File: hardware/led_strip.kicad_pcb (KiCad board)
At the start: 2 copper layers, 30 x 30 mm, 29 parts, among them J1 AKL_5_2, J2 AKL_5_2, J3 AKL_5_2, P1 CON-SENSOR, P2 TST, P3 TST, P4 TST, P5 TST, P6 TST, P7 TST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

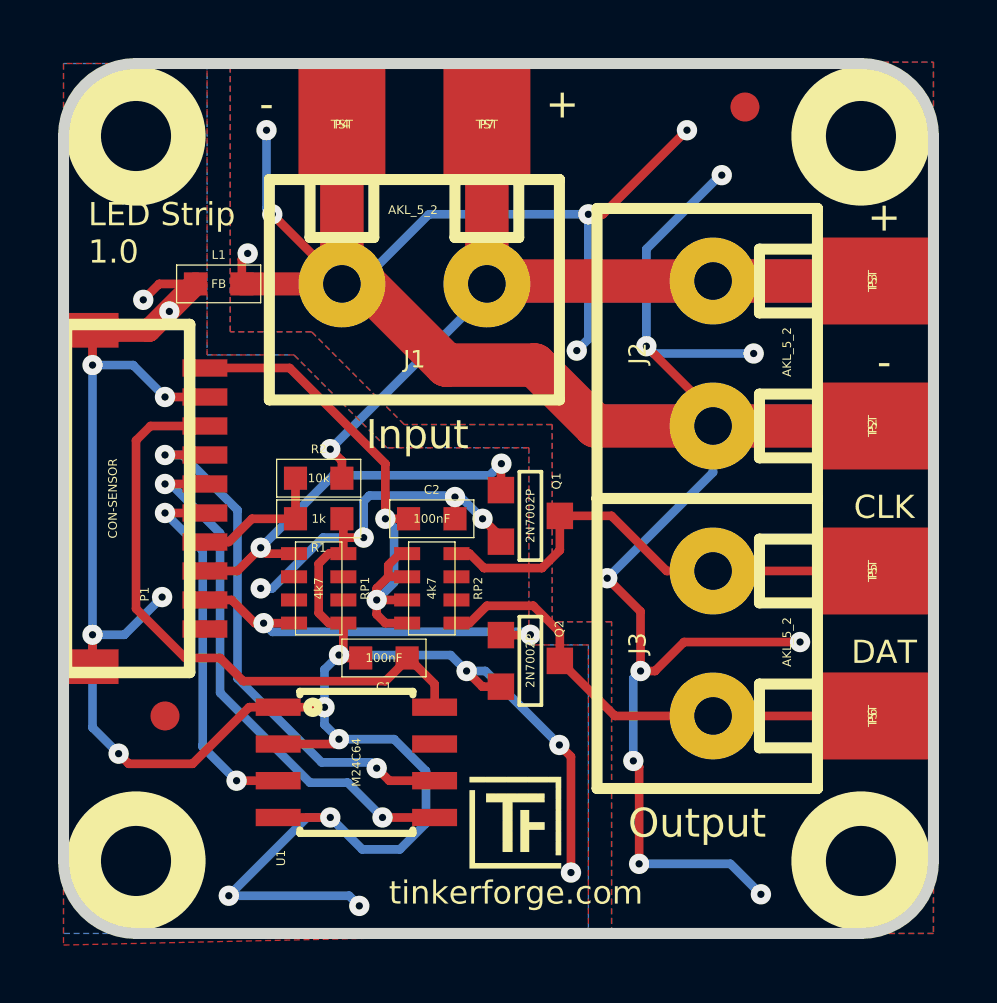
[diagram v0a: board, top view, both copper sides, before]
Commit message: update hardware files with new resistor values
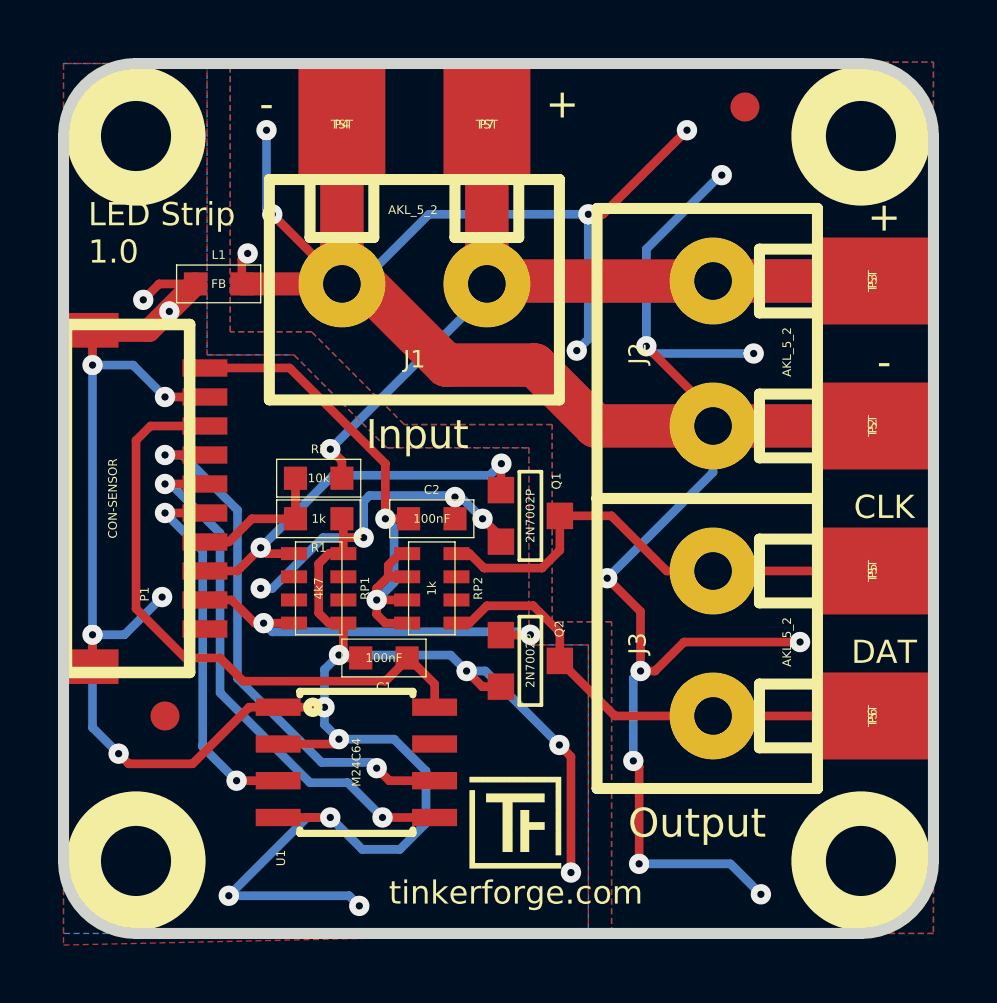
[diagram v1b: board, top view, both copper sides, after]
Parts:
- RP2: value 4k7 -> 1k
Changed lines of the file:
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@@
-(kicad_pcb (version 3) (host pcbnew "(2013-05-18 BZR 4017)-stable")
+(kicad_pcb (version 3) (host pcbnew "(2013-07-24 BZR 4024)-stable")
   (general
     (links 43)
@@
       (effects (font (size 0.29972 0.29972) (thickness 0.0762)))
     )
-    (fp_text value 4k7 (at 0 0 270) (layer F.SilkS)
+    (fp_text value 1k (at 0 0 270) (layer F.SilkS)
       (effects (font (size 0.29972 0.29972) (thickness 0.07493)))
     )

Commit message: new prototype of led strip bricklet
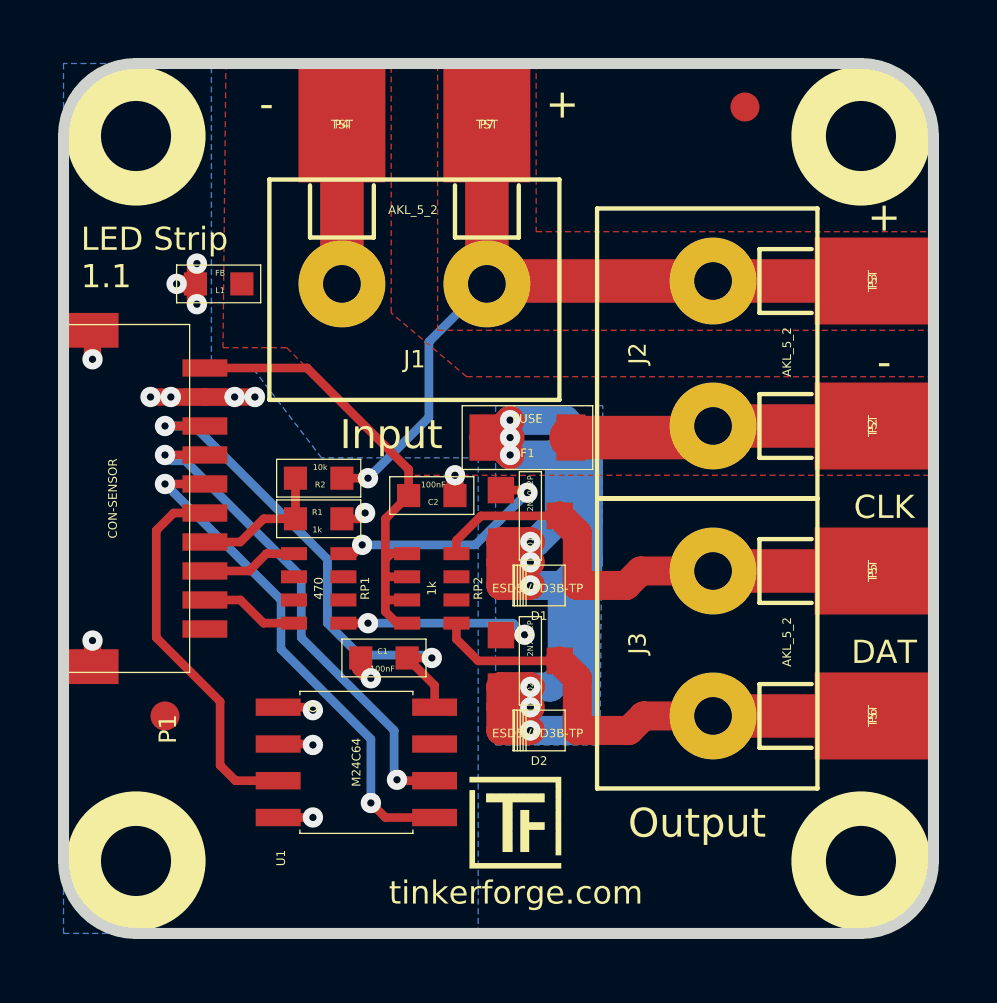
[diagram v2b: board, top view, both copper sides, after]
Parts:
- added D1: ESD5V0D3B-TP, kicad-libraries:SOD-323, F.Cu at (59.3, 45.3)
- added D2: ESD5V0D3B-TP, kicad-libraries:SOD-323, F.Cu at (59.3, 50.3)
- added F1: FUSE, kicad-libraries:1206, F.Cu at (58.9, 40.2)
- C1, C2, L1, R1, R2: footprint 0603 -> kicad-libraries:0603
- J1, J2, J3: footprint AKL_5_2 -> kicad-libraries:AKL_5_2
- P1: footprint CON-SENSOR -> kicad-libraries:CON-SENSOR
- P2, P3, P4, P5, P6, P7: footprint SOLDER_PAD2 -> kicad-libraries:SOLDER_PAD2
- Q1, Q2: footprint SOT23GDS -> kicad-libraries:SOT23GDS
- RP1: value 4k7 -> 470; footprint 4X0603 -> kicad-libraries:4X0603
- RP2: footprint 4X0603 -> kicad-libraries:4X0603
- U1: footprint SOIC8 -> kicad-libraries:SOIC8
- U2, U3, U4, U5: footprint DRILL_NP -> kicad-libraries:DRILL_NP
- moved C2 0.80 mm to (55.6, 42.2)
- moved VAL 0.75 mm to (55.6, 42.3)
- moved VAL 0.20 mm to (61.8, 42.3)
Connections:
- P1 pad 8: N-0000014 -> Net-(P1-Pad8)
- P1 pad 9: N-0000015 -> Net-(P1-Pad9)
- Q1 pad G: N-0000014 -> Net-(Q1-PadG)
- Q1 pad S: GND -> Net-(D1-Pad2)
- Q2 pad G: N-0000015 -> Net-(Q2-PadG)
- Q2 pad S: GND -> Net-(D1-Pad2)
- RP1 pad 1: GND -> Net-(Q1-PadG)
- RP1 pad 4: GND -> Net-(Q2-PadG)
- RP1 pad 5: N-0000015 -> Net-(P1-Pad9)
- RP1 pad 8: N-0000014 -> Net-(P1-Pad8)
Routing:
- net GND: track 99.2 -> 13.7 mm, vias 20 -> 15
- net AGND: track 98.1 -> 16.1 mm, vias 15 -> 0
- net Net-(D1-Pad2): track 0.00 -> 38.5 mm, vias 0 -> 9
- net N-0000014: track 13.9 -> 0.00 mm, vias 2 -> 0
- net N-0000015: track 13.8 -> 0.00 mm, vias 2 -> 0
- net Net-(Q1-PadG): track 0.00 -> 8.17 mm, vias 0 -> 2
- net Net-(Q2-PadG): track 0.00 -> 7.24 mm, vias 0 -> 2
- net Net-(P1-Pad9): track 0.00 -> 3.40 mm
- net Net-(P1-Pad8): track 0.00 -> 3.32 mm
- net VCC: track 21.2 -> 18.1 mm, vias 0 -> 2
- net +5V: track 19.0 -> 17.0 mm, vias 2 -> 0
- net Net-(P1-Pad4): track 18.7 -> 17.5 mm
- net Net-(P1-Pad5): track 18.7 -> 17.7 mm
- net Net-(D2-Pad1): track 16.7 -> 17.5 mm
- net Net-(D1-Pad1): track 16.8 -> 17.4 mm
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- added copper zone on B.Cu, net Net-(D1-Pad2)
- added copper zone on F.Cu, net Net-(J1-Pad2)
- removed copper zone on B.Cu, net AGND
- removed copper zone on F.Cu, net GND
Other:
- board text added: "LED Strip 1.1"
- board text removed: "LED Strip 1.0"

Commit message: drc run
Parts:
- Fiducial_Mark (x2): footprint Fiducial_Mark -> kicad-libraries:Fiducial_Mark

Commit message: Add 3d information (final)
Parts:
- C1, C2, L1: footprint kicad-libraries:0603 -> kicad-libraries:C0603
- F1: footprint kicad-libraries:1206 -> kicad-libraries:F1206
- G***: footprint Logo_31x31 -> kicad-libraries:Logo_31x31
- R1, R2: footprint kicad-libraries:0603 -> kicad-libraries:R0603
- VAL: footprint WEEE_7mm -> kicad-libraries:WEEE_7mm
- VAL: footprint CE_5mm -> kicad-libraries:CE_5mm
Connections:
- P1 pad 10: (no net) -> Net-(P1-Pad10)
- RP1 pad 2: (no net) -> Net-(RP1-Pad2)
- RP1 pad 3: (no net) -> Net-(RP1-Pad3)
- RP1 pad 6: (no net) -> Net-(RP1-Pad6)
- RP1 pad 7: (no net) -> Net-(RP1-Pad7)
- RP2 pad 2: (no net) -> Net-(RP2-Pad2)
- RP2 pad 3: (no net) -> Net-(RP2-Pad3)
- U1 pad 7: (no net) -> Net-(U1-Pad7)

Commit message: specify fuse
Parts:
- F1: value FUSE -> 0ZCJ0035FF2G
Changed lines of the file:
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@@
-(kicad_pcb (version 4) (host pcbnew 4.0.2+dfsg1-stable)
+(kicad_pcb (version 4) (host pcbnew 4.0.7-e2-6376~58~ubuntu17.04.1)
   (general
     (links 46)
     (no_connects 0)
-    (area 42.709499 27.109499 73.090501 57.490501)
+    (area 41.994339 26.394339 282.27147 165.489573)
     (thickness 1.6002)
     (drawings 19)
@@
       (effects (font (size 0.3 0.3) (thickness 0.075)))
     )
-    (fp_text value FUSE (at 0 -0.65) (layer F.Fab)
+    (fp_text value 0ZCJ0035FF2G (at 0 -0.65) (layer F.Fab)
       (effects (font (size 0.3 0.3) (thickness 0.075)))
     )
